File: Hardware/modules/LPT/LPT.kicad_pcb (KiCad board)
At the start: 4 copper layers, 83.3 x 68.2 mm, 22 parts, among them J1 DB25_Receptacle, J2 Bus_PCI_6502, U1 74HC138, U2 74HC138, U3 74HC00, U4 74AHC541, U5 74HCT574, U6 74HCT574, U7 74HC02

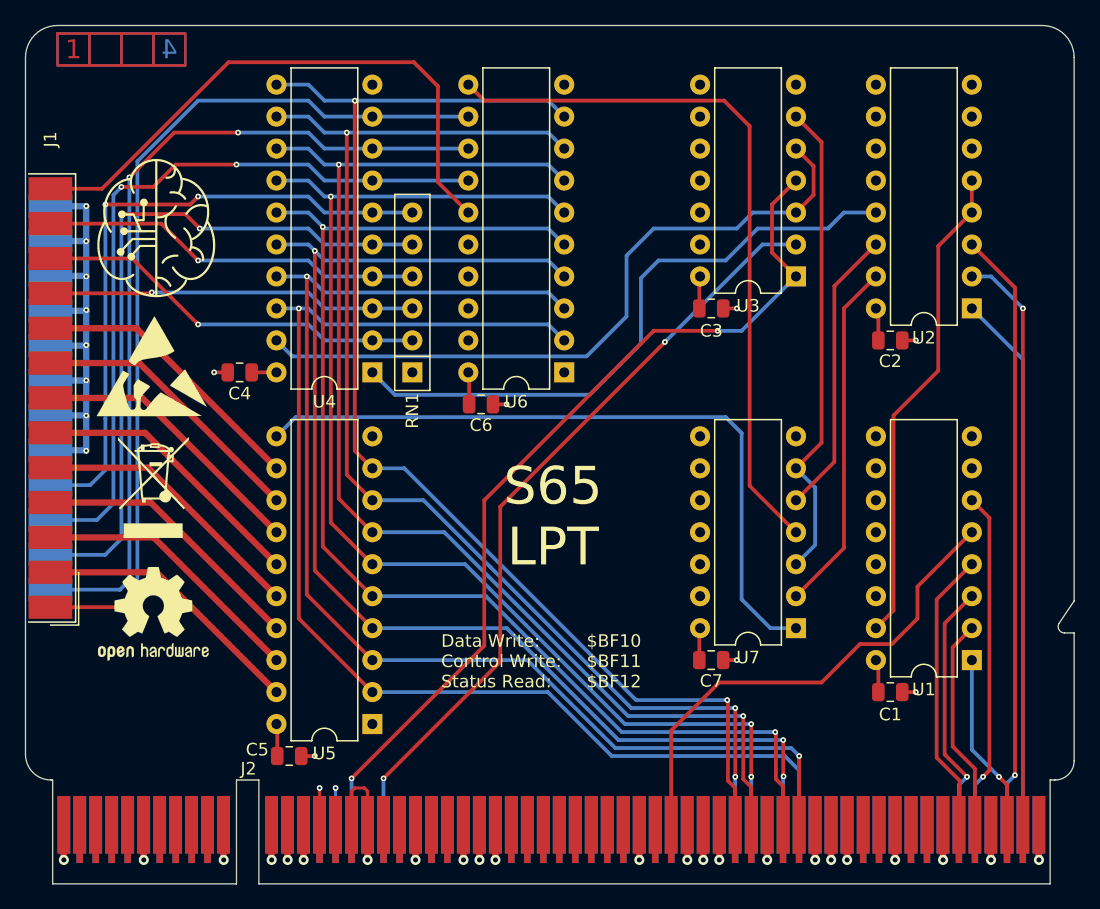
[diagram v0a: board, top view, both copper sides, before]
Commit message: Hardware Update Add MyCPU VGA Module Beautify all Schematics minor Error corrections Readme Update
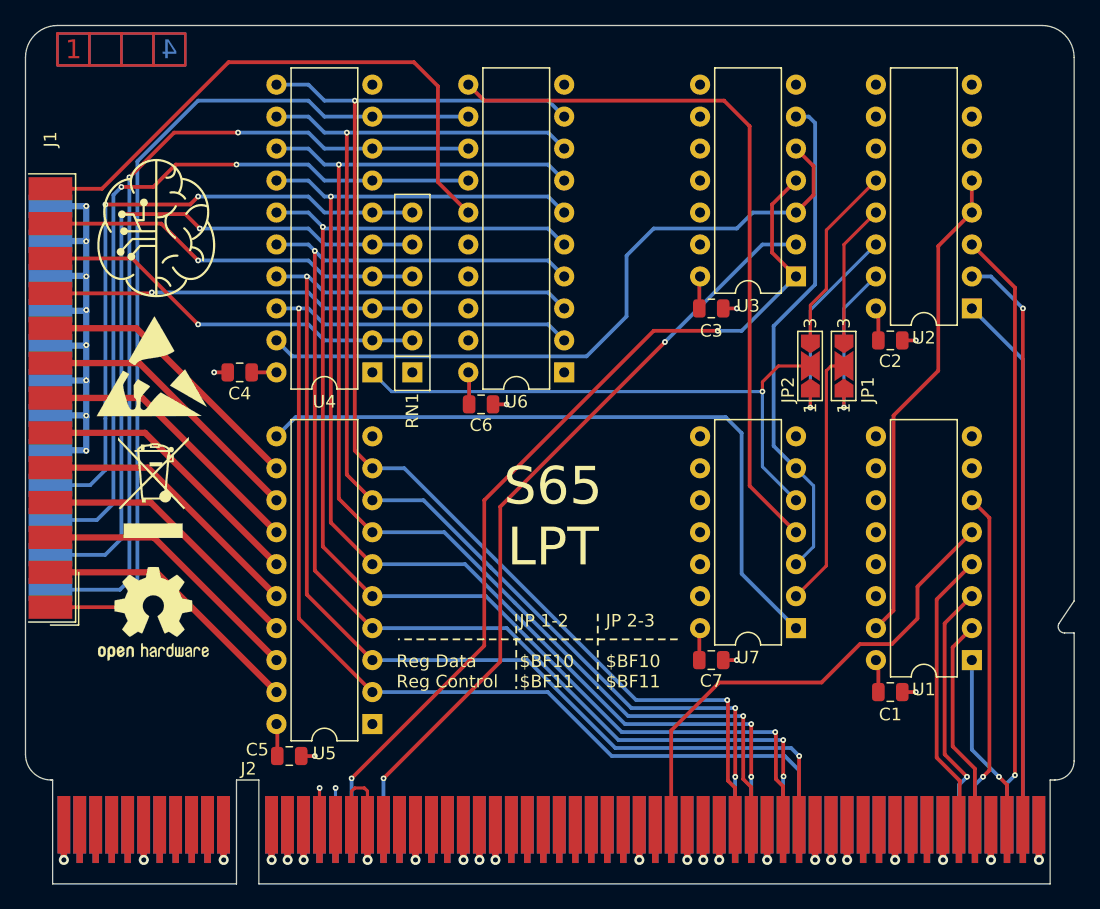
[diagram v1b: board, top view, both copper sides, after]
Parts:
- added JP1: Data, Jumper:SolderJumper-3_P2.0mm_Open_TrianglePad1.0x1.5mm_NumberLabels, F.Cu at (177.2, 85.9)
- added JP2: Control, Jumper:SolderJumper-3_P2.0mm_Open_TrianglePad1.0x1.5mm_NumberLabels, F.Cu at (174.5, 85.9)
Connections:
- J2 pad A11: /A13 -> unconnected-(J2-A13-PadA11)_0
- J2 pad A12: /A15 -> unconnected-(J2-A15-PadA12)_0
- J2 pad A25: /~{ROM} -> unconnected-(J2-~{ROM}-PadA25)
- J2 pad A27: /~{IRQ_0.0} -> unconnected-(J2-~{IRQ_0.0}-PadA27)_0
- J2 pad A28: /~{IRQ_0.1} -> unconnected-(J2-~{IRQ_0.1}-PadA28)
- J2 pad A29: /~{IRQ_0.2} -> unconnected-(J2-~{IRQ_0.2}-PadA29)
- J2 pad A30: /~{IRQ_0.3} -> unconnected-(J2-~{IRQ_0.3}-PadA30)_0
- J2 pad A31: /~{IRQ_0.4} -> unconnected-(J2-~{IRQ_0.4}-PadA31)
- J2 pad A32: /~{IRQ_0.5} -> unconnected-(J2-~{IRQ_0.5}-PadA32)
- J2 pad A33: /~{IRQ_0.6} -> unconnected-(J2-~{IRQ_0.6}-PadA33)
- J2 pad A34: /~{IRQ_0.7} -> unconnected-(J2-~{IRQ_0.7}-PadA34)
- J2 pad A38: /SYNC_VPA -> unconnected-(J2-Sync/VPA-PadA38)_0
- J2 pad A39: /Ø2/VDA -> unconnected-(J2-Ø2/VDA-PadA39)_0
- J2 pad A41: /~{RDY} -> unconnected-(J2-~{RDY}-PadA41)_0
- J2 pad A42: /~{BE} -> unconnected-(J2-~{BE}-PadA42)
- J2 pad A45: /E -> unconnected-(J2-E-PadA45)
- J2 pad A53: /RAM_0 -> unconnected-(J2-RAM0-PadA53)
- J2 pad A54: /RAM_1 -> unconnected-(J2-RAM1-PadA54)_0
- J2 pad A55: /RAM_2 -> unconnected-(J2-RAM2-PadA55)_0
- J2 pad A56: /RAM_3 -> unconnected-(J2-RAM3-PadA56)_0
- J2 pad A58: /RAM_4 -> unconnected-(J2-RAM4-PadA58)
- J2 pad A59: /RAM_5 -> unconnected-(J2-RAM5-PadA59)_0
- J2 pad A60: /RAM_6 -> unconnected-(J2-RAM6-PadA60)
- J2 pad A61: /RAM_7 -> unconnected-(J2-RAM7-PadA61)_0
- J2 pad A8: /A9 -> unconnected-(J2-A9-PadA8)
- J2 pad A9: /A11 -> unconnected-(J2-A11-PadA9)_0
- J2 pad B11: /A12 -> unconnected-(J2-A12-PadB11)_0
- J2 pad B12: /A14 -> unconnected-(J2-A14-PadB12)_0
- J2 pad B24: /~{L_RAM} -> unconnected-(J2-~{L_RAM}-PadB24)_0
- J2 pad B25: /~{H_RAM} -> unconnected-(J2-~{H_RAM}-PadB25)_0
- J2 pad B27: /~{IRQ} -> unconnected-(J2-~{IRQ}-PadB27)
- J2 pad B28: /~{IRQ_0} -> unconnected-(J2-~{IRQ_0}-PadB28)
- J2 pad B29: /~{IRQ_1} -> unconnected-(J2-~{IRQ_1}-PadB29)
- J2 pad B30: /~{IRQ_2} -> unconnected-(J2-~{IRQ_2}-PadB30)_0
- J2 pad B31: /~{IRQ_3} -> unconnected-(J2-~{IRQ_3}-PadB31)_0
- J2 pad B32: /~{IRQ_4} -> unconnected-(J2-~{IRQ_4}-PadB32)
- J2 pad B33: /~{NMI} -> unconnected-(J2-~{NMI}-PadB33)_0
- J2 pad B34: /PAGE -> unconnected-(J2-PAGE_ROM-PadB34)
- J2 pad B38: /~{VP} -> unconnected-(J2-~{VP}-PadB38)_0
- J2 pad B39: /~{ML} -> unconnected-(J2-~{ML}-PadB39)_0
- J2 pad B41: /~{RES} -> unconnected-(J2-~{RES}-PadB41)
- J2 pad B46: /M/X -> unconnected-(J2-M/~{X}-PadB46)
- J2 pad B53: /ROM_0 -> unconnected-(J2-ROM0-PadB53)
- J2 pad B54: /ROM_1 -> unconnected-(J2-ROM1-PadB54)
- J2 pad B55: /ROM_2 -> unconnected-(J2-ROM2-PadB55)
- J2 pad B56: /ROM_3 -> unconnected-(J2-ROM3-PadB56)_0
- J2 pad B58: /ROM_4 -> unconnected-(J2-ROM4-PadB58)
- J2 pad B59: /ROM_5 -> unconnected-(J2-ROM5-PadB59)_0
- J2 pad B60: /ROM_6 -> unconnected-(J2-ROM6-PadB60)
- J2 pad B61: /ROM_7 -> unconnected-(J2-ROM7-PadB61)
- J2 pad B8: /A8 -> unconnected-(J2-A8-PadB8)_0
- J2 pad B9: /A10 -> unconnected-(J2-A10-PadB9)_0
- U2 pad 12: unconnected-(U2-~{Y3}-Pad12) -> Net-(JP2-B)
- U2 pad 13: /~{State} -> Net-(JP1-B)
- U2 pad 14: /~{Control} -> Net-(JP2-A)
- U2 pad 15: /~{Data} -> Net-(JP1-A)
- U4 pad 1: /~{State} -> /~{Control}
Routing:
- net /~{State}: track 49.8 -> 0.00 mm
- net /~{Control}: track 23.0 -> 46.5 mm, vias 0 -> 1
- net Net-(JP2-A): track 0.00 -> 16.4 mm, vias 0 -> 1
- net Net-(JP2-B): track 0.00 -> 14.9 mm
- net Net-(JP1-A): track 0.00 -> 12.8 mm, vias 0 -> 1
- net Net-(JP1-B): track 0.00 -> 11.2 mm
- net /~{Data}: track 28.0 -> 20.5 mm
- net /~{WR}: track 38.5 -> 40.0 mm
- net Net-(U5-Cp): track 56.6 -> 55.4 mm
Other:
- board text added: "JP 1-2 $BF10 $BF11"
- board text added: "JP 2-3 $BF10 $BF11"
- board text added: "Reg Data Reg Control"
- board text removed: "$BF10 $BF11 $BF12"
- board text removed: "Data Write: Control Write: Status Read:"

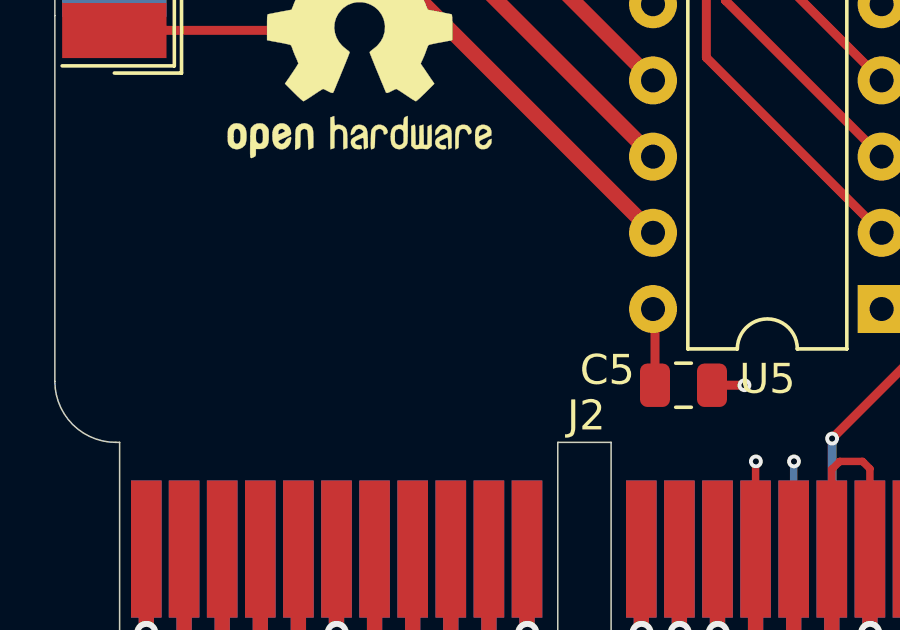
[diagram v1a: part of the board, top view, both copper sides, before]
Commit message: Hardware Review Pt. 1 fix Address Decoding for Strobe Generators add bulk capacitance to every board fix wiring of Prototyping Board
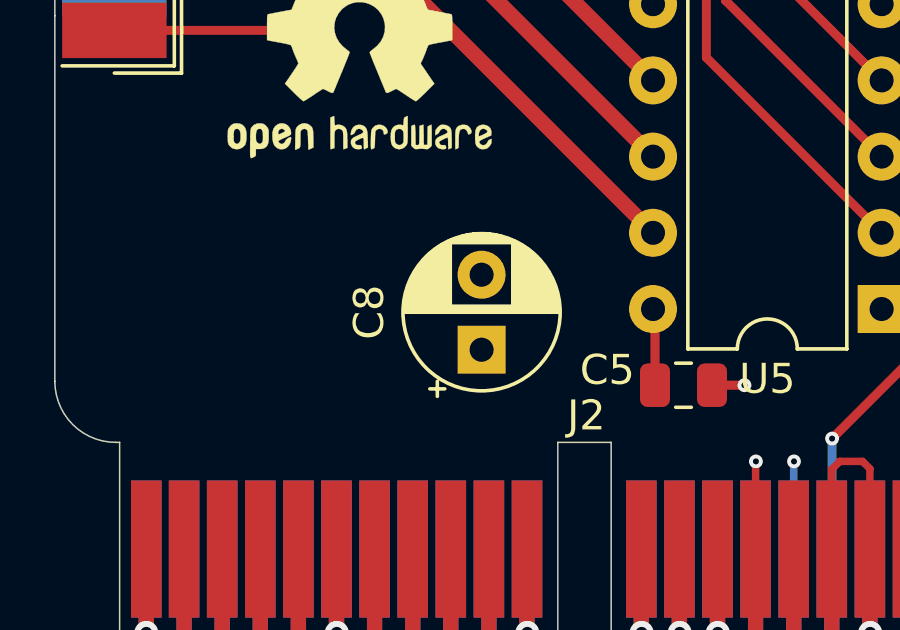
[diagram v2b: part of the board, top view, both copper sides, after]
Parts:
- added C8: 10µ, Capacitor_THT:CP_Radial_D5.0mm_P2.50mm, F.Cu at (126.4, 115.7)

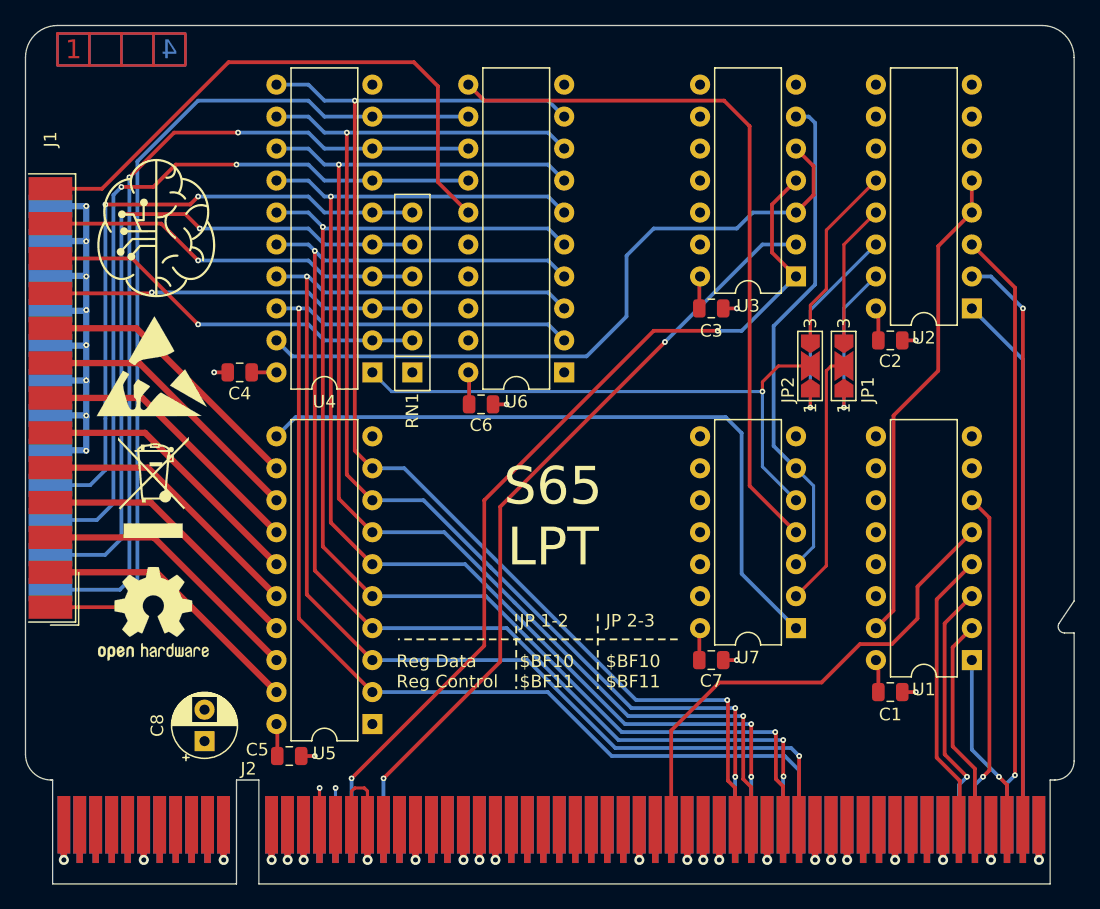
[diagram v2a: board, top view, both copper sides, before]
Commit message: Big Review Update - Changed Copper Pours on all PCBs - Implemented errors found at review - fixed some additional errors
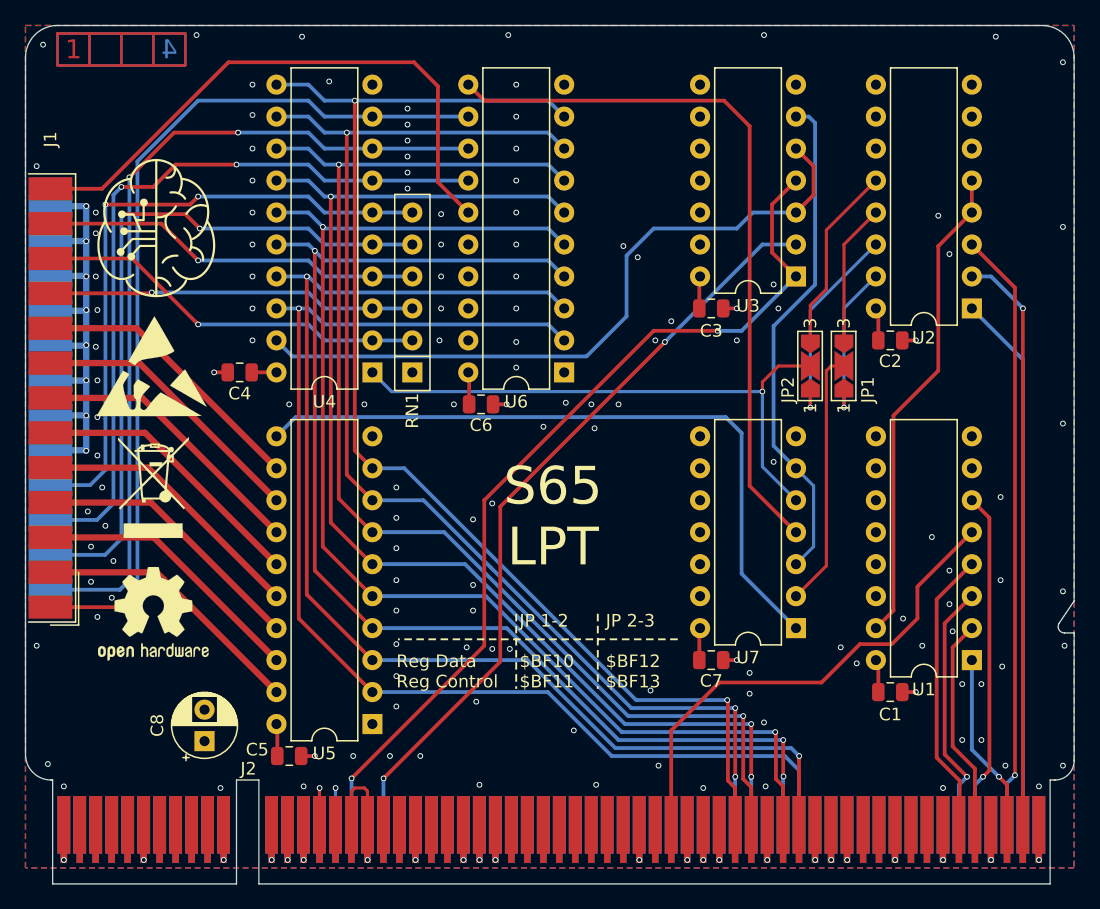
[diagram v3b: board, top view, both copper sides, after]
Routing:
- net +5V: vias 4 -> 134
- added copper zone on B.Cu, net +5V
- added copper zone on F.Cu, net +5V
- added copper zone on In1.Cu, net GND
- removed copper zone on In1.Cu, net +5V
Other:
- board text added: "JP 2-3 $BF12 $BF13"
- board text removed: "JP 2-3 $BF10 $BF11"
